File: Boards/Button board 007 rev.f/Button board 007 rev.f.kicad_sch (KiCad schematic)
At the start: 17 parts, among them J1 Conn_02x25_Odd_Even, U3 7407, U4 7407

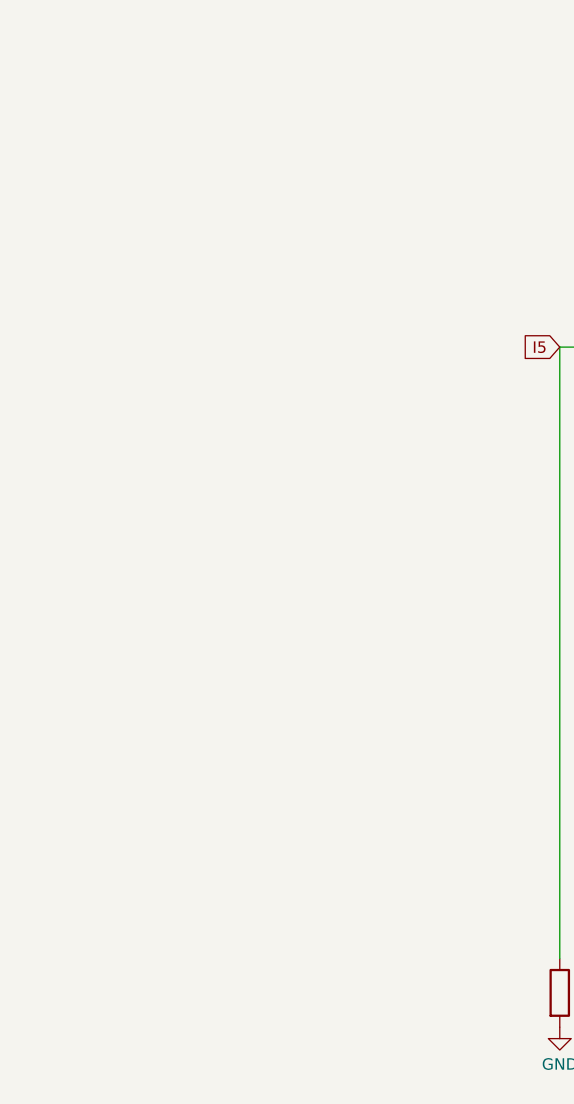
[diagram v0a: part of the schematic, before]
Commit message: button board done
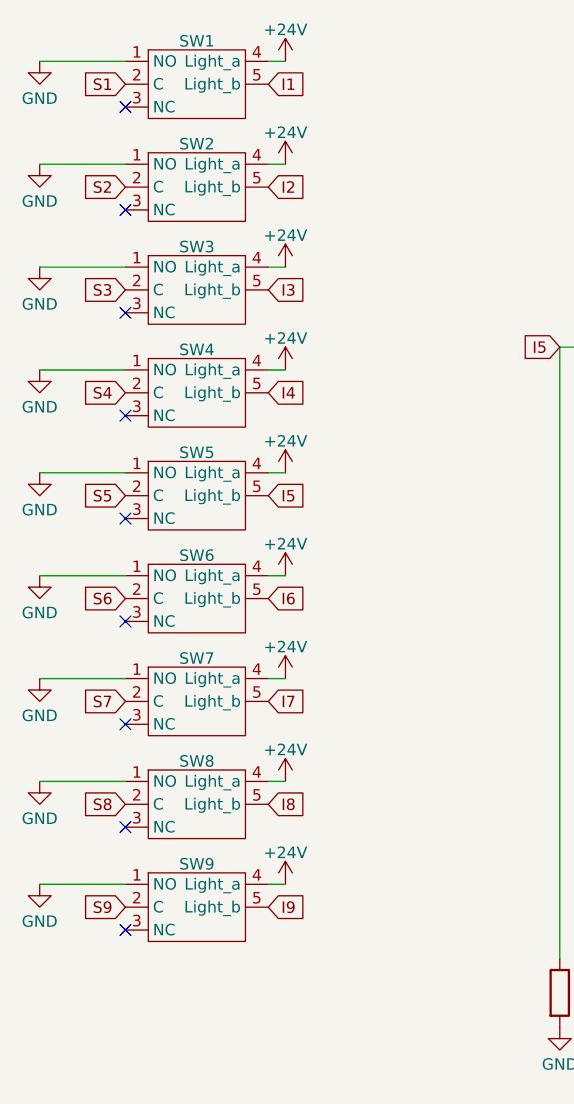
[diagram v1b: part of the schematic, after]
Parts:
- added SW1, SW2, SW3, SW4, SW5, SW6, SW7, SW8, SW9: ~, Evan's parts:chuck e cheese microswitch, symbol Evan's parts:chuck_e_cheese_microswitch
- C1: footprint (none) -> Capacitor_THT:CP_Radial_Tantal_D5.0mm_P5.00mm
- J1: footprint (none) -> Connector_PinHeader_2.54mm:PinHeader_2x25_P2.54mm_Vertical
- R1, R2, R3, R4, R5, R6, R7, R8, R9: footprint (none) -> Resistor_THT:R_Axial_DIN0516_L15.5mm_D5.0mm_P20.32mm_Horizontal
- U3, U4: footprint (none) -> Package_DIP:DIP-14_W7.62mm
- W2: footprint (none) -> Connector_PinHeader_2.54mm:PinHeader_1x02_P2.54mm_Vertical
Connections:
- net +24V: now also SW1.4 (Light_a), SW2.4 (Light_a), SW3.4 (Light_a), SW4.4 (Light_a), SW5.4 (Light_a), SW6.4 (Light_a), SW7.4 (Light_a), SW8.4 (Light_a), SW9.4 (Light_a)
- net GND: now also SW1.1 (NO), SW2.1 (NO), SW3.1 (NO), SW4.1 (NO), SW5.1 (NO), SW6.1 (NO), SW7.1 (NO), SW8.1 (NO), SW9.1 (NO)
- net I1: now also SW1.5 (Light_b)
- net I2: now also SW2.5 (Light_b)
- net I3: now also SW3.5 (Light_b)
- net I4: now also SW4.5 (Light_b)
- net I5: now also SW5.5 (Light_b)
- net I6: now also SW6.5 (Light_b)
- net I7: now also SW7.5 (Light_b)
- net I8: now also SW8.5 (Light_b)
- net I9: now also SW9.5 (Light_b)
- net S1: now also SW1.2 (C)
- net S2: now also SW2.2 (C)
- net S3: now also SW3.2 (C)
- net S4: now also SW4.2 (C)
- net S5: now also SW5.2 (C)
- net S6: now also SW6.2 (C)
- net S7: now also SW7.2 (C)
- net S8: now also SW8.2 (C)
- net S9: now also SW9.2 (C)
- no-connect marks 21 -> 30
